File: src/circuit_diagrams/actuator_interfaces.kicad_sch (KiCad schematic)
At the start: 38 parts, among them J1 BOOT_MDE, J2 DEBUG, J3 Conn_01x04, J4 Conn_01x05, J5 Conn_02x06_Odd_Even, J6 Conn_02x06_Odd_Even, Q1 Si2319CDS, Q2 Si2319CDS, U3 STM32F103CBTx, U4 AP2112K-3.3, U5 PCA9685PW, Y1 Crystal_GND24

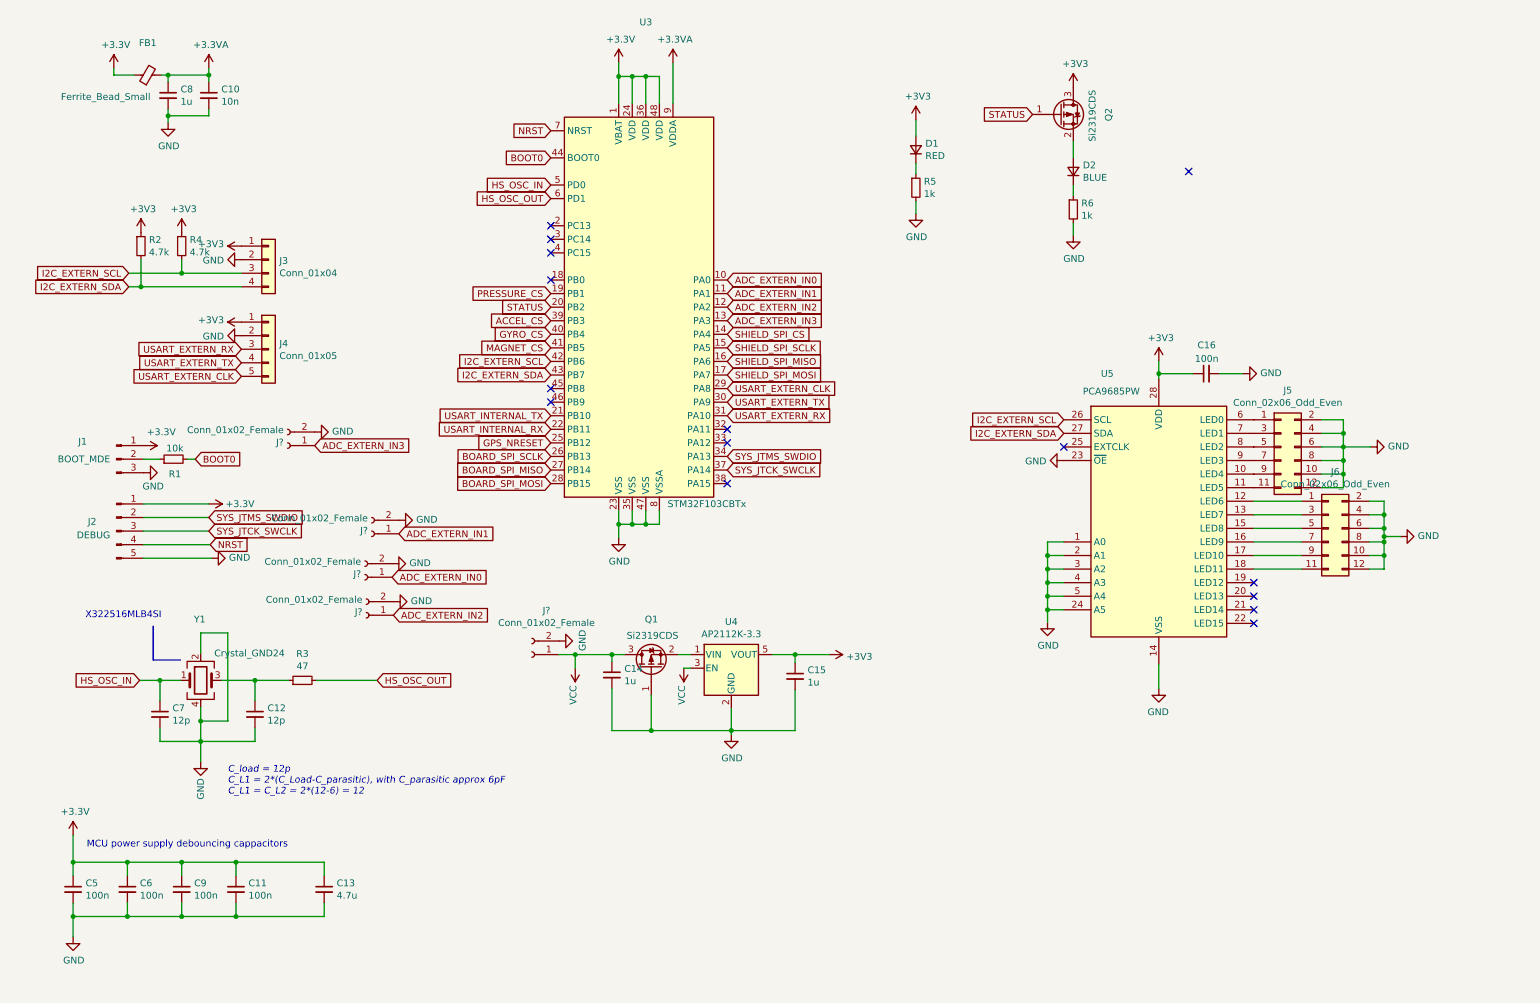
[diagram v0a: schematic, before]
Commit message: [DEVMINOR] Reorganization of the circuit diagram
Adding dividers and labels to subsections of the project
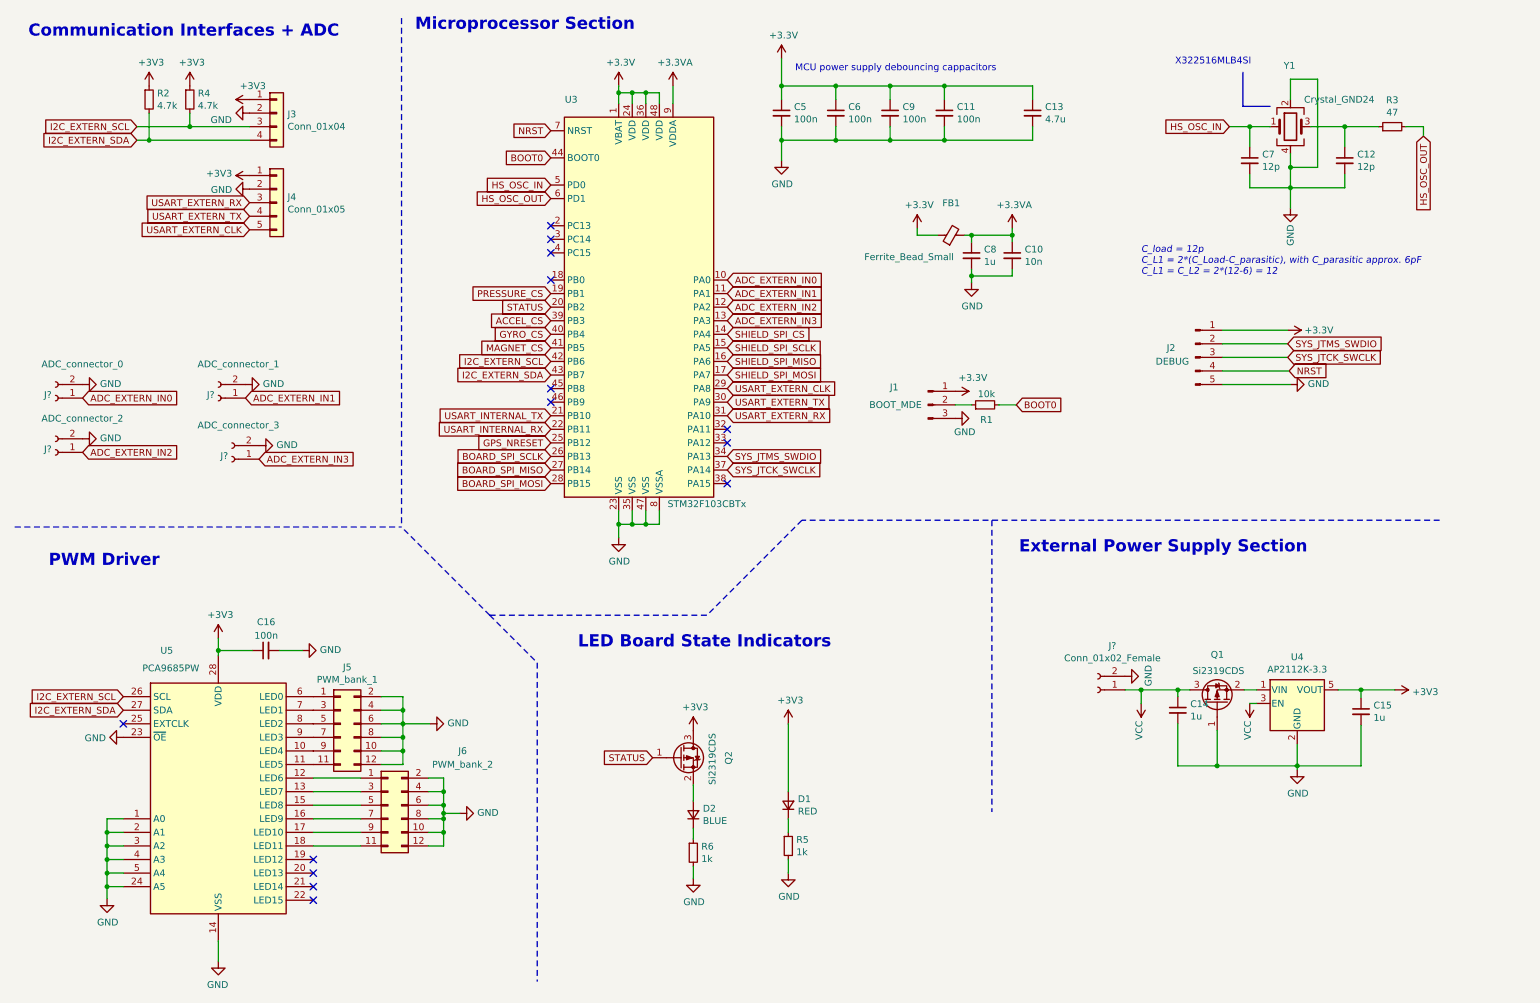
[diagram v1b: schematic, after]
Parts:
- J5: value Conn_02x06_Odd_Even -> PWM_bank_1
- J6: value Conn_02x06_Odd_Even -> PWM_bank_2
- J?: value Conn_01x02_Female -> ADC_connector_0
- J?: value Conn_01x02_Female -> ADC_connector_2
- J?: value Conn_01x02_Female -> ADC_connector_1
- J?: value Conn_01x02_Female -> ADC_connector_3
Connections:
- no-connect marks 15 -> 14
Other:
- note added: "C_load = 12p C_L1 = 2*(C_Load-C_parasitic), with C_parasitic approx. 6pF C_L1 = C_L2 = 2*(12-6) = 12"
- note added: "Communication Interfaces + ADC"
- note added: "External Power Supply Section"
- note added: "LED Board State Indicators"
- note added: "Microprocessor Section"
- note added: "PWM Driver"
- note removed: "C_load = 12p C_L1 = 2*(C_Load-C_parasitic), with C_parasitic approx 6pF C_L1 = C_L2 = 2*(12-6) = 12"
- moved on the sheet: C10, C11, C12, C13, C14, C15, C16, C5, C6, C7, C8, C9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
